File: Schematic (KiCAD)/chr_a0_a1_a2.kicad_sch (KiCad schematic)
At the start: 28 parts, among them P27 INVERT

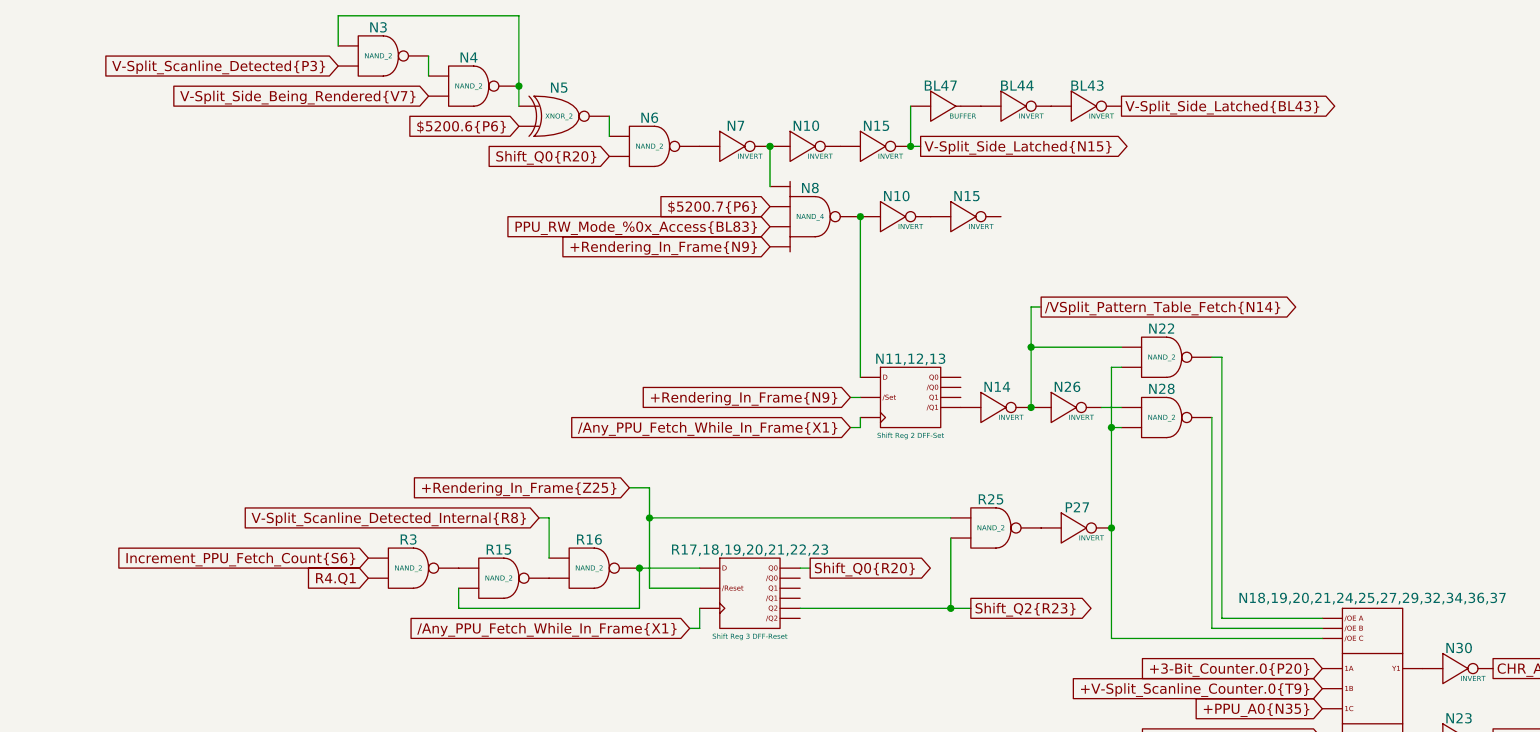
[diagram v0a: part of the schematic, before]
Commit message: - Lots of additional comments and signal name improvements.  - "Don't know what this is yet but it is important" section of the pulse channels:    - I worked out the logic and it is a 4-bit binary up-counter with preload, made from gates and D-latches instead of T-flip-flops.    - It is extremely similar to the envelope counter, but takes twice the die space and much more traces.    - None of its outputs go anywhere else, so I believe that it has no actual function.    - It seems to be a previous attempt at making the envelope counter and it got disconnected and left in.    - Each pulse channel has its own copy and I moved both of them to the "Artifacts" sheet.    - The wasted space amounts to about half of one of the large columns on the left side of the die.  - A couple of "OAI2" cells that noted "unclear order": I determined the correct order of the inputs based on several others which were known.  - Deduced the purpose of the 2 separate methods of scanline detection:    - The one looking for 3 consecutive reads finds the start of a scanline.    - The one counting PPU /RD to find PPU cycle 336, finds the end of the scanline.    - I moved these beside each other on the same sheet for clarity.  - A66.5 Changed from Nand to Nor in order to make sense.  - Basic test mode:    - Pin 92: Active low, enables test mode.    - Pin 29: In test mode, it gives external control of "Scanline Start Detection", which is normally done with the familiar 3 matching PPU reads.  When not in test mode, the pin has no function.    - Pin 30: In test mode, it gives external control of "Scanline End Detection", which is normally done by counting PPU /RD to find PPU cycle 336.  It also gives control of "Pulse Length Clock" when in test mode.  When not in test mode, the pin has no function.    - Pin 98/SL3: In test mode, it gives external control of "Pulse Timer Clock".  Whether or not in test mode, this pin low makes the MMC5 pretend $5104 had not yet been written since reset, probably as a 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
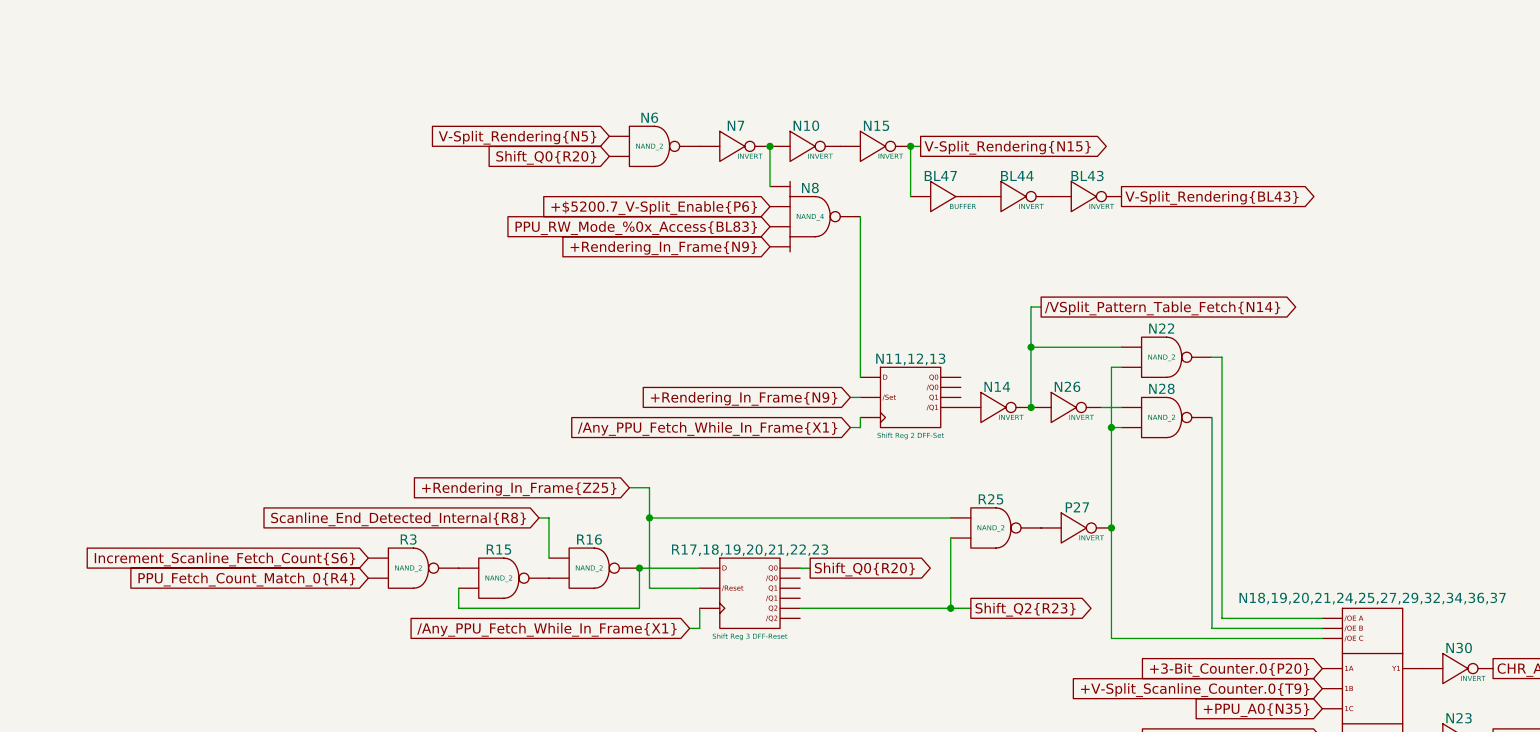
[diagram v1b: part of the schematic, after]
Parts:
- removed N10, N15: INVERT, symbol MMC5:INVERT
- removed N3, N4: NAND_2, symbol MMC5:NAND_2
- removed N5: XNOR_2, symbol MMC5:XNOR_2
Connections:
- net $5200.7{P6} is gone; now on net PPU_RW_Mode_%0x_Access{BL83}: N8. (X)
- net R4.Q1 is gone; now on net PPU_Fetch_Count_Match_0{R4}: R3. (X)
- net V-Split_Scanline_Detected_Internal{R8} is gone; now on net Scanline_End_Detected_Internal{R8}: R16. (X)
- net V-Split_Side_Latched{BL43} is gone; now on net V-Split_Rendering{BL43}: BL43. (X)
- net V-Split_Side_Latched{N15} is gone; now on net V-Split_Rendering{N15}: BL47. (X), N15. (X)
- net at R15. (X): now also R16. (X); no longer R3. (X)
- net Scanline_End_Detected_Internal{R8}: now reaches R16. (X)
- net Scanline_End_Detected_Internal{R8}: no longer R15. (X)
- net at P27. (X): now also N18,19,20,21,24,25,27,29,32,34,36,37. (Y3), N22. (X), N28. (X); no longer R25. (X)
- net V-Split_Rendering{N5}: now reaches N6. (X)
- net at N7. (X): now also N10. (X), N8. (X); no longer N6. (X)
- net at BL44. (X): now also BL43. (X); no longer BL47. (X)
- net at N28. (X): now also N26. (X); no longer N18,19,20,21,24,25,27,29,32,34,36,37. (Y3)
- net V-Split_Rendering{BL43}: now reaches BL43. (X)
- net V-Split_Rendering{BL43}: no longer BL44. (X)
- net V-Split_Rendering{N15}: now reaches N15. (X)
- net V-Split_Rendering{N15}: no longer N10. (X)
- net Increment_PPU_Fetch_Count{S6} renamed PPU_Fetch_Count_Match_0{R4}
- new net: R15. (X), R16. (X), R17,18,19,20,21,22,23. (/Q2)
- new net: R15. (X), R3. (X)
- new net: P27. (X), R25. (X)
- new net: N11,12,13. (/Q1), N14. (X)
- new net: N11,12,13. (/Q1), N8. (X)
- new net: N6. (X), N7. (X)
- new net: BL44. (X), BL47. (X)
- new net: N18,19,20,21,24,25,27,29,32,34,36,37. (Y3), N28. (X)
- new net: N18,19,20,21,24,25,27,29,32,34,36,37. (Y3), N23. (X)
- new net: N17. (X), N18,19,20,21,24,25,27,29,32,34,36,37. (Y3)
- new net: N18,19,20,21,24,25,27,29,32,34,36,37. (Y3), N30. (X)
- new net: N18,19,20,21,24,25,27,29,32,34,36,37. (Y3), N22. (X)
- new net: N10. (X), N15. (X)
- new net +$5200.7_V-Split_Enable{P6}: N8. (X)
- new net Increment_Scanline_Fetch_Count{S6}: R3. (X)
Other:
- moved on the sheet: BL43, BL44, BL47

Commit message: I fixed 2 errors in the letterless MMC5 tracing:
1. BK5 is a NAND-4 gate.  It was thought to be NAND-3 before.
2.  BL83 and BL96 signals got swapped here before.  They actually cross each other:

BL83 = "PPU_RW_Mode_%0x_Access"
BL96 = "+ExRAM_Mode_$0x"

This propagated out to several changes in the schematic.
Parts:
- added DISCH1,2,3: Counter 2 Reset, symbol MMC5:Counter_2_Reset
- added DISCH10, DISCH12, DISCH16, DISCH6, DISCH8, P14, P20, P8: INVERT, symbol MMC5:INVERT
- added DISCH11: BIGBUF, symbol MMC5:BIGBUF
- added DISCH13, DISCH14, DISCH4, DISCH5, DISCH7, DISCH9, J74, P10, P11, P16, P17, P23, P24, R26: NAND_2, symbol MMC5:NAND_2
- added DISCH15: AOI_2, symbol MMC5:AOI_2
- added DISCH17: Oscillator, symbol MMC5:Oscillator
- added J72: NAND_4, symbol MMC5:NAND_4
- added J73: NOR_2, symbol MMC5:NOR_2
- added P12,13,18,19,25,26: Reg 3 DFF-Reset, symbol MMC5:Reg_3_DFF-Reset
- added P15, P21, P9: T-FF Preload, symbol MMC5:T-FF_Preload
- added P22, P28, R28: BUFFER, symbol MMC5:BUFFER
- added R27: D-FF Reset, symbol MMC5:D-FF_Reset
- added R29: INVERT_2, symbol MMC5:INVERT_2
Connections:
- net PPU_RW_Mode_%0x_Access{BL83} is gone; now on net +Rendering_In_Frame{N9}: N8. (X)
- net +3-Bit_Counter.0{P20}: now also P20. (X)
- net +3-Bit_Counter.1{P14}: now also P14. (X)
- net +3-Bit_Counter.2{P8}: now also P8. (X)
- net at R15. (X): now also R16. (X); no longer R3. (X)
- net at P27. (X): now also N18,19,20,21,24,25,27,29,32,34,36,37. (Y3), N22. (X), N28. (X); no longer R25. (X)
- net at N7. (X): now also N10. (X), N8. (X); no longer N6. (X)
- net at BL44. (X): now also BL43. (X); no longer BL47. (X)
- net at N28. (X): now also N26. (X); no longer N18,19,20,21,24,25,27,29,32,34,36,37. (Y3)
- new net: DISCH11. (X), DISCH14. (X), DISCH4. (X), DISCH5. (X), DISCH7. (X), DISCH9. (X)
- new net: DISCH5. (X), DISCH6. (X)
- new net: R27. (/Q), R28. (X)
- new net: R27. (/Q), R29. (X)
- new net: R26. (X), R27. (/Q)
- new net: DISCH7. (X), DISCH8. (X)
- new net: R15. (X), R16. (X), R17,18,19,20,21,22,23. (/Q2)
- new net: R15. (X), R3. (X)
- new net: P10. (X), P11. (X), P9. (/Q)
- new net: P27. (X), R25. (X)
- new net: P12,13,18,19,25,26. (Q2), P28. (X)
- new net: P12,13,18,19,25,26. (Q2), P17. (X)
- new net: P11. (X), P12,13,18,19,25,26. (Q2)
- new net: P12,13,18,19,25,26. (Q2), P24. (X)
- new net: P14. (X), P15. (/Q), P9. (/Q)
- new net: P8. (X), P9. (/Q)
- new net: P21. (/Q), P22. (X)
- new net: DISCH10. (X), DISCH9. (X)
- new net: N11,12,13. (/Q1), N14. (X)
- new net: N11,12,13. (/Q1), N8. (X)
- new net: N6. (X), N7. (X)
- new net: P15. (/Q), P16. (X), P17. (X)
- new net: P28. (X), R26. (X)
- new net: DISCH15. (X), DISCH16. (X), DISCH17. (X)
- new net: DISCH15. (X), DISCH16. (X)
- new net: DISCH15. (X), DISCH4. (X)
- new net: P21. (/Q), P23. (X), P24. (X)
- new net: BL44. (X), BL47. (X)
- new net: N18,19,20,21,24,25,27,29,32,34,36,37. (Y3), N28. (X)
- new net: P15. (/Q), P20. (X), P21. (/Q)
- new net: R26. (X), R29. (X)
- new net: N18,19,20,21,24,25,27,29,32,34,36,37. (Y3), N23. (X)
- new net: N17. (X), N18,19,20,21,24,25,27,29,32,34,36,37. (Y3)
- new net: N18,19,20,21,24,25,27,29,32,34,36,37. (Y3), N30. (X)
- new net: N18,19,20,21,24,25,27,29,32,34,36,37. (Y3), N22. (X)
- new net: DISCH1,2,3. (Q1), DISCH12. (X)
- new net: N10. (X), N15. (X)
- new net: DISCH12. (X), DISCH13. (X)
- new net: DISCH13. (X), DISCH14. (X)
- new net: DISCH11. (X), DISCH14. (X)
- new net +$2006_2nd_Write{DISCH3}: DISCH1,2,3. (Q1), DISCH4. (X)
- new net +CPU_$2006_Access{J73}: J73. (X), J74. (X)
- new net +CPU_$2xxx{J54}: J72. (X)
- new net +CPU_$x0xx{J50}: J72. (X)
- new net +CPU_$xx0x{K90}: J72. (X)
- new net +CPU_$xxx6{J22}: J72. (X)
- new net +ExRAM_Mode_$0x{BL96}: N8. (X)
- new net +Reg_Write{L111}: J74. (X)
- new net 3-bit_Reload_0: DISCH10. (X), DISCH9. (X), P21. (/Q), P23. (X)
- new net 3-bit_Reload_1: DISCH7. (X), DISCH8. (X), P15. (/Q), P16. (X)
- new net 3-bit_Reload_2: DISCH5. (X), DISCH6. (X), P10. (X), P9. (/Q)
- new net Scanline_End_Detected{P3}: DISCH15. (X), P22. (X)
- new net /CPU_$2002_RD{L110}: DISCH13. (X), R28. (X)
- new net /CPU_$2005_WR{L113}: R29. (X)
- new net /CPU_$2006_WR{J74}: DISCH1,2,3. (Q1), J74. (X)
- new net /CPU_$2006{J72}: J72. (X), J73. (X)
- new net /CPU_D0{X18}: P12,13,18,19,25,26. (Q2)
- new net /CPU_D1{X19}: P12,13,18,19,25,26. (Q2)
- new net /CPU_D2{X20}: P12,13,18,19,25,26. (Q2)
- new net /Reg_Access{K98}: J73. (X)
- new net /Rendering_In_Frame{R24}: P10. (X), P11. (X), P16. (X), P17. (X), P23. (X), P24. (X)
- new net /Reset_Detect{P29}: P12,13,18,19,25,26. (Q2)
- new net /Scanline_Start_Detected{AA3}: DISCH15. (X)
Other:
- note added: "$2005 Register 2nd Write Snooping"
- note added: "$2006 Register 2nd Write Snooping"
- note added: "/Q -> D turns this into a T-FF with async /reset."
- note added: ">>> Theory: this signal oscillates during H-blank, continuously triggering the 3-bit counter to reload."
- note added: "Fine Vertical Scroll 3-Bit Scanline Counter"
- note added: "MMC5 Only"
- note added: "MMC5A Only"
- note added: "Resyncs 2nd write tracking when $2002 is read."
- note added: "The counter counts: 0,1,2,3,0,1,2,3... So Q1 is high for: 2nd, 3rd, 6th, 7th, 10th, 11th... writes."
- note added: "Theory: /OE C Active when: - PPU is fetching sprite pattern data or not rendering (ex. via PPUDATA). /OE B Active when: - PPU is fetching background pattern data in V-Split region. /OE A Active when: - PPU is fetching background pattern data everywhere else."
- moved on the sheet: BL43, BL44, BL47, N10, N11,12,13, N14, N15, N17, N18,19,20,21,24,25,27,29,32,34,36,37, N22, N23, N26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

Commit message: Schematic and SVG Updates
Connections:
- net at R27. (/Q): now also R26. (X)
- net at R26. (X): now also R29. (X); no longer R27. (/Q)
- net at R15. (X): now also R16. (X); no longer R3. (X)
- net +OE_B_V-Split_Counter{N29}: now reaches P27. (X)
- net +OE_B_V-Split_Counter{N29}: now also N18,19,20,21,24,25,27,29,32,34,36,37. (Y3), N22. (X), N28. (X); no longer R25. (X)
- net /OE_B_V-Split_Counter{N28}: now reaches N18,19,20,21,24,25,27,29,32,34,36,37. (Y3), N28. (X)
- net /OE_B_V-Split_Counter{N28}: no longer N22. (X), P27. (X)
- net at P28. (X): now also R26. (X); no longer P12,13,18,19,25,26. (Q2)
- net at N7. (X): now also N8. (X); no longer N6. (X)
- net at BL44. (X): now also BL43. (X); no longer BL47. (X)
- net at DISCH12. (X): now also DISCH13. (X); no longer DISCH1,2,3. (Q1)
- net at DISCH14. (X): now also DISCH11. (X); no longer DISCH13. (X)
- new net: DISCH11. (X), DISCH14. (X), DISCH4. (X), DISCH5. (X), DISCH7. (X), DISCH9. (X)
- new net: DISCH5. (X), DISCH6. (X)
- new net: R27. (/Q), R28. (X)
- new net: R27. (/Q), R29. (X)
- new net: DISCH7. (X), DISCH8. (X)
- new net: R15. (X), R16. (X), R17,18,19,20,21,22,23. (/Q2)
- new net: R15. (X), R3. (X)
- new net: P10. (X), P11. (X), P9. (/Q)
- new net: P27. (X), R25. (X)
- new net: P12,13,18,19,25,26. (Q2), P28. (X)
- new net: P12,13,18,19,25,26. (Q2), P17. (X)
- new net: P11. (X), P12,13,18,19,25,26. (Q2)
- new net: P12,13,18,19,25,26. (Q2), P24. (X)
- new net: P14. (X), P15. (/Q), P9. (/Q)
- new net: P8. (X), P9. (/Q)
- new net: P21. (/Q), P22. (X)
- new net: DISCH10. (X), DISCH9. (X)
- new net: N11,12,13. (/Q1), N14. (X)
- new net: N10. (X), N11,12,13. (/Q1), N8. (X)
- new net: N6. (X), N7. (X)
- new net: P15. (/Q), P16. (X), P17. (X)
- new net: DISCH15. (X), DISCH16. (X), DISCH17. (X)
- new net: DISCH15. (X), DISCH4. (X)
- new net: P21. (/Q), P23. (X), P24. (X)
- new net: BL44. (X), BL47. (X)
- new net: N26. (X), N28. (X)
- new net: P15. (/Q), P20. (X), P21. (/Q)
- new net: N18,19,20,21,24,25,27,29,32,34,36,37. (Y3), N23. (X)
- new net: N17. (X), N18,19,20,21,24,25,27,29,32,34,36,37. (Y3)
- new net: N18,19,20,21,24,25,27,29,32,34,36,37. (Y3), N30. (X)
- new net: DISCH1,2,3. (Q1), DISCH12. (X)
- new net: DISCH13. (X), DISCH14. (X)
- new net 1: N18,19,20,21,24,25,27,29,32,34,36,37. (Y3), N22. (X)
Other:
- note added: "N29 is an internal buffer of the multiplexer."
- note added: "Never Enables 3-bit Counter"
- note added: "Seemingly, none of this new stuff has any effect because the 3-bit scanline counter can't be enabled onto CHR A0/A1/A2."
- moved on the sheet: BL43, BL44, BL47, N10, N15, N17, N18,19,20,21,24,25,27,29,32,34,36,37, N23, N30, N6, N7, N8

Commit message: Tracing and schematic updates.  - Added timer to schematic.  - Added all items from artifacts sheet to the MMC5A trace.
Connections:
- net V-Split_Rendering{BL43} is gone; now on net /V-Split_Rendering{BL43}: BL43. (X)
- net at R27. (/Q): now also R26. (X)
- net at R26. (X): now also R29. (X); no longer R27. (/Q)
- net at R15. (X): now also R16. (X); no longer R3. (X)
- net at P28. (X): now also R26. (X); no longer P12,13,18,19,25,26. (Q2)
- net at N7. (X): now also N8. (X); no longer N6. (X)
- net at BL44. (X): now also BL43. (X); no longer BL47. (X)
- net /V-Split_Rendering{BL43}: now reaches BL43. (X)
- net /V-Split_Rendering{BL43}: no longer BL44. (X)
- net at DISCH12. (X): now also DISCH13. (X); no longer DISCH1,2,3. (Q1)
- net at DISCH14. (X): now also DISCH11. (X); no longer DISCH13. (X)
- net V-Split_Rendering{N15} renamed /V-Split_Rendering{N15}
- new net: DISCH11. (X), DISCH14. (X), DISCH4. (X), DISCH5. (X), DISCH7. (X), DISCH9. (X)
- new net: DISCH5. (X), DISCH6. (X)
- new net: R27. (/Q), R28. (X)
- new net: R27. (/Q), R29. (X)
- new net: DISCH7. (X), DISCH8. (X)
- new net: R15. (X), R16. (X), R17,18,19,20,21,22,23. (/Q2)
- new net: R15. (X), R3. (X)
- new net: P10. (X), P11. (X), P9. (/Q)
- new net: P27. (X), R25. (X)
- new net: P12,13,18,19,25,26. (Q2), P28. (X)
- new net: P12,13,18,19,25,26. (Q2), P17. (X)
- new net: P11. (X), P12,13,18,19,25,26. (Q2)
- new net: P12,13,18,19,25,26. (Q2), P24. (X)
- new net: P14. (X), P15. (/Q), P9. (/Q)
- new net: P8. (X), P9. (/Q)
- new net: P21. (/Q), P22. (X)
- new net: DISCH10. (X), DISCH9. (X)
- new net: N11,12,13. (/Q1), N14. (X)
- new net: N10. (X), N11,12,13. (/Q1), N8. (X)
- new net: N6. (X), N7. (X)
- new net: P15. (/Q), P16. (X), P17. (X)
- new net: DISCH15. (X), DISCH16. (X), DISCH17. (X)
- new net: DISCH15. (X), DISCH4. (X)
- new net: P21. (/Q), P23. (X), P24. (X)
- new net: BL44. (X), BL47. (X)
- new net: N26. (X), N28. (X)
- new net: P15. (/Q), P20. (X), P21. (/Q)
- new net: N18,19,20,21,24,25,27,29,32,34,36,37. (Y3), N23. (X)
- new net: N17. (X), N18,19,20,21,24,25,27,29,32,34,36,37. (Y3)
- new net: N18,19,20,21,24,25,27,29,32,34,36,37. (Y3), N30. (X)
- new net: DISCH1,2,3. (Q1), DISCH12. (X)
- new net: DISCH13. (X), DISCH14. (X)
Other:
- note added: "This area should be verified because it seems N15 should also go low for extended attribute fetches."
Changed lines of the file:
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@@
+		)
+	)
+	(text "This area should be verified because\nit seems N15 should also go low for\nextended attribute fetches."
+		(exclude_from_sim no)
+		(at 122.174 38.354 0)
+		(effects
+			(font
+				(size 1.27 1.27)
+			)
+			(justify left)
 		)
 	)
@@
 		)
 	)
-	(global_label "V-Split_Rendering{BL43}"
+	(global_label "{slash}V-Split_Rendering{BL43}"
 		(shape output)
 		(at 162.56 48.26 0)
@@
 		)
 		(property "Intersheetrefs" "${INTERSHEET_REFS}"
-			(at 189.3727 48.26 0)
+			(at 190.7032 48.26 0)
 			(effects
 				(font
@@
 		)
 	)
-	(global_label "V-Split_Rendering{N15}"
+	(global_label "{slash}V-Split_Rendering{N15}"
 		(shape output)
 		(at 137.16 53.34 0)
@@
 		)
 		(property "Intersheetrefs" "${INTERSHEET_REFS}"
-			(at 163.0051 53.34 0)
-			(effects
-				(font
+			(at 164.3356 53.34 0)
+			(effects
+				(font
